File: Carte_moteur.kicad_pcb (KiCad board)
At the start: 2 copper layers, 94 parts, among them J101 Conn_01x02_Socket, J102 Conn_01x02, J103 Conn_01x02, J201 Conn_01x04_Pin, J301 Conn_01x04_Pin, J401 Conn_01x04_Pin, J601 Conn_01x06_Pin, J602 USB_B_Mini, Q601 MMBTA44, SW201 SW_DIP_x02, SW301 SW_DIP_x02, SW401 SW_DIP_x02, U101 LD1117S33TR_SOT223, U201 TMC2209, U301 TMC2209, U401 TMC2209, U501 STM32G474RETx, U601 ECMF02-2AMX6, U602 LD1117S33TR_SOT223, U603 STM32F103CBTx, Y601 Crystal_GND24

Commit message: Add net class
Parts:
- removed SW201, SW401: SW_DIP_x02, Button_Switch_THT:SW_DIP_SPSTx02_Slide_9.78x7.26mm_W7.62mm_P2.54mm
- added J104: Conn_01x07, Connector_Molex:Molex_KK-254_AE-6410-07A_1x07_P2.54mm_Vertical, F.Cu at (-344.4, -25.7)
- added J202: Conn_01x04_Pin, Connector_Molex:Molex_KK-254_AE-6410-04A_1x04_P2.54mm_Vertical, F.Cu at (-275.7, 52.7)
- added J302: Conn_01x04_Pin, Connector_Molex:Molex_KK-254_AE-6410-04A_1x04_P2.54mm_Vertical, F.Cu at (-299.4, 52.7)
- added J402: Conn_01x04_Pin, Connector_Molex:Molex_KK-254_AE-6410-04A_1x04_P2.54mm_Vertical, F.Cu at (-252.1, 52.7)
- added R101: R_US, Resistor_SMD:R_0603_1608Metric_Pad0.98x0.95mm_HandSolder, F.Cu at (-344.5, -20.5)
- added R102: R_US, Resistor_SMD:R_0603_1608Metric_Pad0.98x0.95mm_HandSolder, F.Cu at (-344.5, -18.0)
- added R103: R_US, Resistor_SMD:R_0603_1608Metric_Pad0.98x0.95mm_HandSolder, F.Cu at (-344.5, -15.5)
- added R104: R_US, Resistor_SMD:R_0603_1608Metric_Pad0.98x0.95mm_HandSolder, F.Cu at (-344.5, -13.0)
- added R105: R_US, Resistor_SMD:R_0603_1608Metric_Pad0.98x0.95mm_HandSolder, F.Cu at (-344.5, -10.5)
- added R206: R_US, Resistor_SMD:R_0805_2012Metric_Pad1.20x1.40mm_HandSolder, B.Cu at (-275.0, 19.4)
- added R207: R_US, Resistor_SMD:R_0603_1608Metric_Pad0.98x0.95mm_HandSolder, B.Cu at (-274.7, 33.9)
- added R306: R_US, Resistor_SMD:R_0805_2012Metric_Pad1.20x1.40mm_HandSolder, B.Cu at (-298.6, 19.4)
- added R307: R_US, Resistor_SMD:R_0603_1608Metric_Pad0.98x0.95mm_HandSolder, B.Cu at (-298.4, 33.9)
- added R406: R_US, Resistor_SMD:R_0805_2012Metric_Pad1.20x1.40mm_HandSolder, B.Cu at (-251.3, 19.4)
- added R407: R_US, Resistor_SMD:R_0603_1608Metric_Pad0.98x0.95mm_HandSolder, B.Cu at (-251.1, 33.9)
- added R512: R_US, Resistor_SMD:R_0603_1608Metric_Pad0.98x0.95mm_HandSolder, F.Cu at (-287.7, -15.3)
- added R513: R_US, Resistor_SMD:R_0603_1608Metric_Pad0.98x0.95mm_HandSolder, F.Cu at (-283.3, -25.4)
- added R514: R_US, Resistor_SMD:R_0603_1608Metric_Pad0.98x0.95mm_HandSolder, F.Cu at (-283.3, -22.9)
- added R515: R_US, Resistor_SMD:R_0603_1608Metric_Pad0.98x0.95mm_HandSolder, F.Cu at (-283.3, -20.4)
- added R516: R_US, Resistor_SMD:R_0603_1608Metric_Pad0.98x0.95mm_HandSolder, F.Cu at (-283.3, -17.8)
- added R517: R_US, Resistor_SMD:R_0603_1608Metric_Pad0.98x0.95mm_HandSolder, F.Cu at (-283.3, -15.3)
- added R518: R_US, Resistor_SMD:R_0805_2012Metric_Pad1.20x1.40mm_HandSolder, F.Cu at (-281.7, -12.6)
- added R519: R_US, Resistor_SMD:R_0805_2012Metric_Pad1.20x1.40mm_HandSolder, F.Cu at (-281.7, -9.66)
- added SW302: SW_DIP_x02, Button_Switch_THT:SW_DIP_SPSTx02_Slide_9.78x7.26mm_W7.62mm_P2.54mm, F.Cu at (-302.5, 19.6)
- added SW303: SW_DIP_x02, Button_Switch_THT:SW_DIP_SPSTx02_Slide_9.78x7.26mm_W7.62mm_P2.54mm, F.Cu at (-255.2, 19.6)
- C201, C202, C301, C302, C401, C402, R202, R205, R302, R305, R402, R405: moved to B.Cu
- C502: footprint Capacitor_SMD:C_0603_1608Metric_Pad1.08x0.95mm_HandSolder -> Capacitor_SMD:C_0805_2012Metric_Pad1.18x1.45mm_HandSolder
- C503: footprint Capacitor_SMD:C_0805_2012Metric_Pad1.18x1.45mm_HandSolder -> Capacitor_SMD:C_0603_1608Metric_Pad1.08x0.95mm_HandSolder
- J201, J301, J401: value Conn_01x04_Pin -> Conn_01x05_Pin; footprint Connector_Molex:Molex_KK-254_AE-6410-04A_1x04_P2.54mm_Vertical -> Connector_Molex:Molex_KK-254_AE-6410-05A_1x05_P2.54mm_Vertical
- R201, R204, R301, R304, R401, R404: footprint Resistor_SMD:R_0805_2012Metric_Pad1.20x1.40mm_HandSolder -> Resistor_SMD:R_0603_1608Metric_Pad0.98x0.95mm_HandSolder; moved to B.Cu
- R203, R303, R403: footprint Resistor_SMD:R_0603_1608Metric_Pad0.98x0.95mm_HandSolder -> Resistor_SMD:R_0805_2012Metric_Pad1.20x1.40mm_HandSolder; moved to B.Cu
- R509, R510, R511: footprint Resistor_SMD:R_0805_2012Metric_Pad1.20x1.40mm_HandSolder -> Resistor_SMD:R_0603_1608Metric_Pad0.98x0.95mm_HandSolder
- moved R511 221.2 mm to (-322.7, -23.3)
- moved R510 221.1 mm to (-322.7, -25.8)
- moved R509 221.0 mm to (-322.7, -28.3)
- moved C104 188.7 mm to (-301.8, -42.3)
- moved C506 183.5 mm to (-296.4, -15.3)
- moved C507 183.4 mm to (-292.0, -25.4)
- moved C505 183.4 mm to (-296.4, -17.8)
- moved C504 183.2 mm to (-296.4, -20.4)
- moved C503 183.1 mm to (-296.4, -22.9)
- moved R501 181.7 mm to (-292.0, -22.9)
- moved R504 181.7 mm to (-292.0, -15.3)
- moved R301 176.5 mm to (-303.9, 7.75), turned to 180 degrees
- moved C105 176.1 mm to (-286.5, -48.5)
- moved R302 171.5 mm to (-303.9, 11.3), turned to 180 degrees
- moved R304 168.8 mm to (-298.4, 31.4)
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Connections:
- net /micro/DIR1 renamed /micro/HRTIM_CHA2
- net /micro/DIR2 renamed /micro/HRTIM_CHB2
- net /micro/DIR3 renamed /micro/HRTIM_CHE2
- net /micro/SPI_MISO renamed /micro/SPI1_MISO
- net /micro/SPI_MOSI renamed /micro/SPI1_MOSI
- net /micro/SPI_SCK renamed /micro/SPI1_SCK
- net /micro/STEP1 renamed /micro/HRTIM_CHA1
- net /micro/STEP2 renamed /micro/HRTIM_CHB1
- net /micro/STEP3 renamed /micro/HRTIM_CHE1
- C502 pad 1: +3V3 -> Net-(U501-VREF+)
- C503 pad 1: Net-(U501-VREF+) -> +3V3
- J201 pad 1: /tmc_motor/A02 -> Net-(J201-Pin_1)
- J201 pad 2: /tmc_motor/A01 -> /micro/TIM1_CH1
- J201 pad 3: /tmc_motor/B01 -> /micro/TIM1_CH2
- J201 pad 4: /tmc_motor/B02 -> /micro/TIM1_ETR
- J301 pad 1: /tmc_motor1/A02 -> Net-(J301-Pin_1)
- J301 pad 2: /tmc_motor1/A01 -> /micro/TIM3_CH1
- J301 pad 3: /tmc_motor1/B01 -> /micro/TIM3_CH2
- J301 pad 4: /tmc_motor1/B02 -> /micro/TIM3_ETR
- J401 pad 1: /tmc_motor2/A02 -> Net-(J401-Pin_1)
- J401 pad 2: /tmc_motor2/A01 -> /micro/TIM5_CH1
- J401 pad 3: /tmc_motor2/B01 -> /micro/TIM5_CH2
- J401 pad 4: /tmc_motor2/B02 -> /micro/TIM5_ETR
- R201 pad 1: +3V3 -> Net-(J201-Pin_1)
- R201 pad 2: Net-(U201-MS1) -> +3V3
- R202 pad 1: Net-(U201-MS1) -> Net-(J201-Pin_1)
- R202 pad 2: GND -> +5V
- R203 pad 1: /micro/TMC1 -> +3V3
- R203 pad 2: Net-(R203-Pad2) -> Net-(U201-MS1)
- R204 pad 1: +3V3 -> Net-(U201-MS1)
- R204 pad 2: Net-(U201-MS2) -> GND
- R205 pad 1: Net-(U201-MS2) -> /micro/TMC1
- R205 pad 2: GND -> Net-(R205-Pad2)
- R301 pad 1: +3V3 -> Net-(J301-Pin_1)
- R301 pad 2: Net-(U301-MS1) -> +3V3
- R302 pad 1: Net-(U301-MS1) -> Net-(J301-Pin_1)
- R302 pad 2: GND -> +5V
- R303 pad 1: /micro/TMC2 -> +3V3
- R303 pad 2: Net-(R303-Pad2) -> Net-(U301-MS1)
- R304 pad 1: +3V3 -> Net-(U301-MS1)
- R304 pad 2: Net-(U301-MS2) -> GND
- R305 pad 1: Net-(U301-MS2) -> /micro/TMC2
- R305 pad 2: GND -> Net-(R305-Pad2)
- R401 pad 1: +3V3 -> Net-(J401-Pin_1)
- R401 pad 2: Net-(U401-MS1) -> +3V3
- R402 pad 1: Net-(U401-MS1) -> Net-(J401-Pin_1)
- R402 pad 2: GND -> +5V
- R403 pad 1: /micro/TMC3 -> +3V3
- R403 pad 2: Net-(R403-Pad2) -> Net-(U401-MS1)
- R404 pad 1: +3V3 -> Net-(U401-MS1)
- R404 pad 2: Net-(U401-MS2) -> GND
- R405 pad 1: Net-(U401-MS2) -> /micro/TMC3
- R405 pad 2: GND -> Net-(R405-Pad2)
- R501 pad 1: /stlink/T_NRST -> /micro/TIM1_CH1
- R502 pad 1: /micro/TMC3 -> /micro/TIM3_CH1
- R502 pad 2: /micro/UART1_TX -> +3V3
- R503 pad 1: /micro/TMC3 -> /micro/TIM5_CH1
- R503 pad 2: /micro/UART1_RX -> +3V3
- R504 pad 1: Net-(U501-VREF+) -> /micro/TIM1_CH2
- R505 pad 1: /micro/TMC1 -> /micro/TIM3_CH2
- R505 pad 2: /micro/UART2_TX -> +3V3
- R506 pad 1: /micro/TMC1 -> /micro/TIM5_CH2
- R506 pad 2: /micro/UART2_RX -> +3V3
- R507 pad 1: /micro/TMC2 -> /micro/TIM1_ETR
- R507 pad 2: /micro/UART3_TX -> +3V3
- R508 pad 1: /micro/TMC2 -> /micro/TIM3_ETR
- R508 pad 2: /micro/UART3_RX -> +3V3
- R509 pad 1: /micro/TMC1 -> /micro/TIM5_ETR
- R509 pad 2: Net-(R509-Pad2) -> +3V3
- R510 pad 1: /micro/TMC2 -> /micro/T_RST
- R510 pad 2: Net-(R509-Pad2) -> +3V3
- R511 pad 1: /micro/TMC3 -> Net-(U501-VREF+)
- R511 pad 2: Net-(R509-Pad2) -> +3V3
- SW301 pad 1: Net-(U301-MS1) -> Net-(U201-MS2)
- SW301 pad 2: Net-(U301-MS2) -> Net-(U201-MS1)
- U201 pad 4: Net-(R203-Pad2) -> Net-(R205-Pad2)
- U301 pad 4: Net-(R303-Pad2) -> Net-(R305-Pad2)
- U401 pad 4: Net-(R403-Pad2) -> Net-(R405-Pad2)
- U501 pad 12: unconnected-(U501-PA0-Pad12) -> /micro/TIM5_CH1
- U501 pad 13: unconnected-(U501-PA1-Pad13) -> /micro/TIM5_CH2
- U501 pad 17: /micro/UART2_RX -> /micro/LPUART1_RX
- U501 pad 18: unconnected-(U501-PA4-Pad18) -> /micro/TIM3_CH2
- U501 pad 33: /micro/UART3_RX -> /micro/LPUART1_TX
- U501 pad 34: unconnected-(U501-PB12-Pad34) -> /micro/TIM5_ETR
- U501 pad 38: unconnected-(U501-PC6-Pad38) -> /micro/TIM3_CH1
- U501 pad 46: unconnected-(U501-PA12-Pad46) -> /micro/TIM1_ETR
- U501 pad 49: /stlink/T_JTMS -> /micro/T_SWDIO
- U501 pad 50: /stlink/T_JTCK -> /micro/T_SWCLK
- U501 pad 51: /stlink/T_JTDI -> /micro/T_JDTI
- U501 pad 55: unconnected-(U501-PD2-Pad55) -> /micro/TIM3_ETR
- U501 pad 56: /stlink/T_SWO -> /micro/T_SWO
- U501 pad 57: unconnected-(U501-PB4-Pad57) -> /micro/UART2_RX
- U501 pad 61: unconnected-(U501-PB8-Pad61) -> /micro/UART3_RX
- U501 pad 7: /stlink/T_NRST -> /micro/T_RST
- U501 pad 8: /micro/LPUART1_RX -> /micro/TIM1_CH1
- U501 pad 9: /micro/LPUART1_TX -> /micro/TIM1_CH2
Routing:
- net GND: track 74.3 -> 148.1 mm
- net /tmc_motor2/A02: track 0.00 -> 52.3 mm
- net /tmc_motor2/A01: track 0.00 -> 43.3 mm
- net /tmc_motor2/B01: track 0.00 -> 35.7 mm
- net +3V3: track 0.00 -> 34.4 mm
- net Net-(U401-MS2): track 0.00 -> 30.7 mm
- net /tmc_motor2/B02: track 0.00 -> 26.4 mm
- net /tmc_motor1/A02: track 0.00 -> 26.2 mm
- net /tmc_motor/A02: track 0.00 -> 26.2 mm
- net Net-(U201-MS2): track 0.00 -> 25.3 mm
- net Net-(U301-MS2): track 0.00 -> 25.3 mm
- net Net-(U401-MS1): track 0.00 -> 23.8 mm
- net /tmc_motor1/A01: track 0.00 -> 21.7 mm
- net /tmc_motor/A01: track 0.00 -> 21.7 mm
- net Net-(U301-MS1): track 0.00 -> 18.2 mm
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
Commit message: move encoder pull up resistor to tmc sheet
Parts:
- removed R501, R502, R503, R504, R505, R506, R507, R508, R509: R_US, Resistor_SMD:R_0603_1608Metric_Pad0.98x0.95mm_HandSolder
- added R210: R_US, Resistor_SMD:R_0603_1608Metric_Pad0.98x0.95mm_HandSolder, B.Cu at (93.0, 135.1)
- added R211: R_US, Resistor_SMD:R_0603_1608Metric_Pad0.98x0.95mm_HandSolder, B.Cu at (95.5, 135.1)
- added R212: R_US, Resistor_SMD:R_0603_1608Metric_Pad0.98x0.95mm_HandSolder, B.Cu at (98.1, 135.1)
- added R523: R_US, Resistor_SMD:R_0603_1608Metric_Pad0.98x0.95mm_HandSolder, B.Cu at (120.5, 134.9)
- added R524: R_US, Resistor_SMD:R_0603_1608Metric_Pad0.98x0.95mm_HandSolder, B.Cu at (123.1, 134.9)
- added R525: R_US, Resistor_SMD:R_0603_1608Metric_Pad0.98x0.95mm_HandSolder, B.Cu at (125.6, 134.9)
- added R526: R_US, Resistor_SMD:R_0603_1608Metric_Pad0.98x0.95mm_HandSolder, B.Cu at (146.8, 134.8)
- added R527: R_US, Resistor_SMD:R_0603_1608Metric_Pad0.98x0.95mm_HandSolder, B.Cu at (149.4, 134.8)
- added R528: R_US, Resistor_SMD:R_0603_1608Metric_Pad0.98x0.95mm_HandSolder, B.Cu at (151.9, 134.8)
- R101, R102, R103, R104, R105: moved to B.Cu
- moved R608 511.0 mm to (115.5, 97.8), turned to 0 degrees
- moved C608 510.1 mm to (118.2, 104.1), turned to 180 degrees
- moved R607 509.9 mm to (115.5, 99.3), turned to 180 degrees
- moved R609 508.9 mm to (115.5, 100.8), turned to 0 degrees
- moved C605 507.8 mm to (115.5, 102.3), turned to 180 degrees
- moved Y601 507.7 mm to (117.8, 106.8), turned to -90 degrees
- moved C609 505.5 mm to (117.5, 109.4), turned to 0 degrees
- moved R613 500.8 mm to (113.2, 108.4), turned to 180 degrees
- moved R610 500.2 mm to (106.1, 96.7), turned to 180 degrees
- moved C607 499.8 mm to (109.4, 103.1), turned to 180 degrees
- moved R614 499.6 mm to (113.2, 110.2), turned to 180 degrees
- moved C603 498.7 mm to (109.4, 104.6), turned to 180 degrees
- moved U603 497.7 mm to (107.8, 103.4), turned to 180 degrees
- moved C606 496.4 mm to (106.1, 102.1), turned to 0 degrees
- moved D601 495.6 mm to (101.2, 95.0), turned to 90 degrees
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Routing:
- net +3V3: track 34.4 -> 156.9 mm
- net +BATT: track 15.7 -> 63.2 mm
- net /micro/T_JDTI: track 0.00 -> 40.5 mm, vias 0 -> 1
- net /micro/T_SWDIO: track 0.00 -> 38.1 mm, vias 0 -> 2
- net /micro/T_SWO: track 0.00 -> 34.8 mm, vias 0 -> 2
- net /micro/T_SWCLK: track 0.00 -> 33.6 mm, vias 0 -> 2
- net GND: track 148.1 -> 120.7 mm
- net /tmc_motor2/A02: track 52.3 -> 25.1 mm
- net /tmc_motor2/A01: track 43.3 -> 21.0 mm
- net /stlink/T_SWO: track 0.00 -> 19.9 mm, vias 0 -> 1
- net /tmc_motor2/B01: track 35.7 -> 16.9 mm
- net /stlink/T_JTMS: track 3.19 -> 21.5 mm, vias 0 -> 1
- net Net-(U401-MS2): track 30.7 -> 15.5 mm
- net /stlink/T_NRST: track 3.21 -> 17.9 mm, vias 0 -> 1
- net /tmc_motor2/B02: track 26.4 -> 12.8 mm
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
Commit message: hrtim
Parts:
- removed R205, R305, R405: R_US, Resistor_SMD:R_0603_1608Metric_Pad0.98x0.95mm_HandSolder
- moved R517 46.8 mm to (186.9, 117.1)
- moved R516 44.6 mm to (180.6, 114.6)
- moved R518 36.1 mm to (154.2, 110.0)
- moved C502 36.1 mm to (159.5, 117.9)
- moved R519 36.1 mm to (159.5, 114.9)
- moved R513 30.8 mm to (145.4, 85.6)
- moved R512 23.7 mm to (144.8, 89.2)
- moved R406 10.6 mm to (147.2, 136.8), turned to 180 degrees
- moved R306 8.55 mm to (118.9, 136.8), turned to 180 degrees
- moved R206 8.41 mm to (91.2, 136.8), turned to 180 degrees
- moved R403 8.34 mm to (147.2, 139.3), turned to 180 degrees
- moved R514 8.07 mm to (175.8, 67.3)
- moved R515 8.07 mm to (175.8, 69.8)
- moved SW303 7.97 mm to (143.7, 136.8), turned to 0 degrees
- moved U501 6.62 mm to (129.5, 105.2), turned to 45 degrees
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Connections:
- U201 pad 4: Net-(R205-Pad2) -> /micro/TMC1
- U301 pad 4: Net-(R305-Pad2) -> /micro/TMC2
- U401 pad 4: Net-(R405-Pad2) -> /micro/TMC3
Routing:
- net GND: track 120.7 -> 260.7 mm
- net /micro/HRTIM_CHA2: track 0.00 -> 126.3 mm, vias 0 -> 3
- net /micro/HRTIM_CHA1: track 0.00 -> 123.8 mm, vias 0 -> 3
- net +BATT: track 63.2 -> 164.4 mm
- net /micro/HRTIM_CHB2: track 0.00 -> 100.1 mm, vias 0 -> 3
- net /micro/HRTIM_CHB1: track 0.00 -> 93.7 mm, vias 0 -> 3
- net /micro/HRTIM_CHE2: track 0.00 -> 71.3 mm, vias 0 -> 1
- net /micro/HRTIM_CHE1: track 0.00 -> 68.2 mm, vias 0 -> 1
- net /micro/TIM1_CH1: track 3.16 -> 36.9 mm, vias 0 -> 2
- net /micro/TIM1_CH2: track 3.16 -> 35.2 mm, vias 0 -> 2
- net /micro/TMC3: track 0.00 -> 30.6 mm, vias 0 -> 1
- net /micro/TMC2: track 0.00 -> 30.4 mm, vias 0 -> 1
- net /micro/TMC1: track 0.00 -> 30.3 mm, vias 0 -> 1
- net +3V3: track 156.9 -> 139.0 mm, vias 0 -> 1
- net /micro/TIM5_CH1: track 3.16 -> 15.6 mm, vias 0 -> 2
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
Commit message: AHHHAHAHAHHAH
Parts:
- added J105: Conn_01x02_Socket, Connector_Molex:Molex_KK-396_A-41791-0002_1x02_P3.96mm_Vertical, F.Cu at (166.6, 119.9)
- moved R514 70.7 mm to (122.2, 113.4), turned to 90 degrees
- moved R515 67.9 mm to (123.7, 113.4), turned to 90 degrees
- moved R517 54.3 mm to (136.4, 97.3), turned to 180 degrees
- moved R511 48.4 mm to (126.7, 114.8), turned to 90 degrees
- moved R516 48.2 mm to (136.4, 95.2), turned to 180 degrees
- moved C504 26.0 mm to (138.9, 107.0), turned to 90 degrees
- moved R513 24.1 mm to (123.7, 96.0), turned to -90 degrees
- moved R512 23.9 mm to (121.9, 96.0), turned to -90 degrees
- moved C503 16.8 mm to (122.8, 89.7), turned to 180 degrees
- moved R519 12.7 mm to (146.8, 115.6)
- moved C506 12.3 mm to (127.0, 95.0), turned to 90 degrees
- moved C505 11.9 mm to (131.8, 95.0), turned to 90 degrees
- moved C502 9.99 mm to (149.6, 119.1)
- moved J101 9.68 mm to (166.7, 108.9)
- moved C602 7.80 mm to (84.3, 103.3)
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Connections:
- J301 pad 2: /micro/TIM3_CH1 -> /micro/TIM5_CH1
- J301 pad 3: /micro/TIM3_CH2 -> /micro/TIM5_CH2
- J301 pad 4: /micro/TIM3_ETR -> /micro/TIM5_ETR
- J401 pad 2: /micro/TIM5_CH1 -> /micro/TIM3_CH1
- J401 pad 3: /micro/TIM5_CH2 -> /micro/TIM3_CH2
- J401 pad 4: /micro/TIM5_ETR -> /micro/TIM3_ETR
- R514 pad 1: /micro/TMC3 -> /micro/TMC2
- R515 pad 1: /micro/TMC3 -> /micro/TMC2
- R516 pad 1: /micro/TMC2 -> /micro/TMC3
- R517 pad 1: /micro/TMC2 -> /micro/TMC3
- R523 pad 1: /micro/TIM3_CH1 -> /micro/TIM5_CH1
- R524 pad 1: /micro/TIM3_CH2 -> /micro/TIM5_CH2
- R525 pad 1: /micro/TIM3_ETR -> /micro/TIM5_ETR
- R526 pad 1: /micro/TIM5_CH1 -> /micro/TIM3_CH1
- R527 pad 1: /micro/TIM5_CH2 -> /micro/TIM3_CH2
- R528 pad 1: /micro/TIM5_ETR -> /micro/TIM3_ETR
- U301 pad 7: /micro/HRTIM_CHB1 -> /micro/HRTIM_CHE1
- U301 pad 8: /micro/HRTIM_CHB2 -> /micro/HRTIM_CHE2
- U401 pad 7: /micro/HRTIM_CHE1 -> /micro/HRTIM_CHB1
- U401 pad 8: /micro/HRTIM_CHE2 -> /micro/HRTIM_CHB2
- U501 pad 30: /micro/UART3_TX -> unconnected-(U501-PB10-Pad30)
- U501 pad 62: unconnected-(U501-PB9-Pad62) -> /micro/UART3_TX
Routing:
- net +3V3: track 139.0 -> 61.1 mm, vias 1 -> 0
- net /micro/TIM1_ETR: track 3.16 -> 60.9 mm
- net +BATT: track 164.4 -> 110.8 mm
- net GND: track 260.7 -> 208.0 mm
- net /micro/HRTIM_CHB2: track 100.1 -> 58.2 mm, vias 3 -> 1
- net /micro/TIM3_ETR: track 3.27 -> 43.3 mm
- net /micro/HRTIM_CHB1: track 93.7 -> 56.5 mm, vias 3 -> 1
- net /micro/TMC3: track 30.6 -> 63.3 mm
- net /micro/T_JDTI: track 33.7 -> 2.64 mm
- net /micro/TMC2: track 30.4 -> 0.00 mm, vias 1 -> 0
- net /micro/TMC1: track 30.3 -> 0.00 mm, vias 1 -> 0
- net /micro/T_SWO: track 31.0 -> 2.54 mm, vias 2 -> 0
- net /micro/T_SWDIO: track 30.5 -> 2.64 mm, vias 2 -> 0
- net /micro/TIM1_CH1: track 36.9 -> 63.1 mm, vias 2 -> 1
- net /micro/TIM3_CH1: track 3.16 -> 27.8 mm, vias 1 -> 0
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
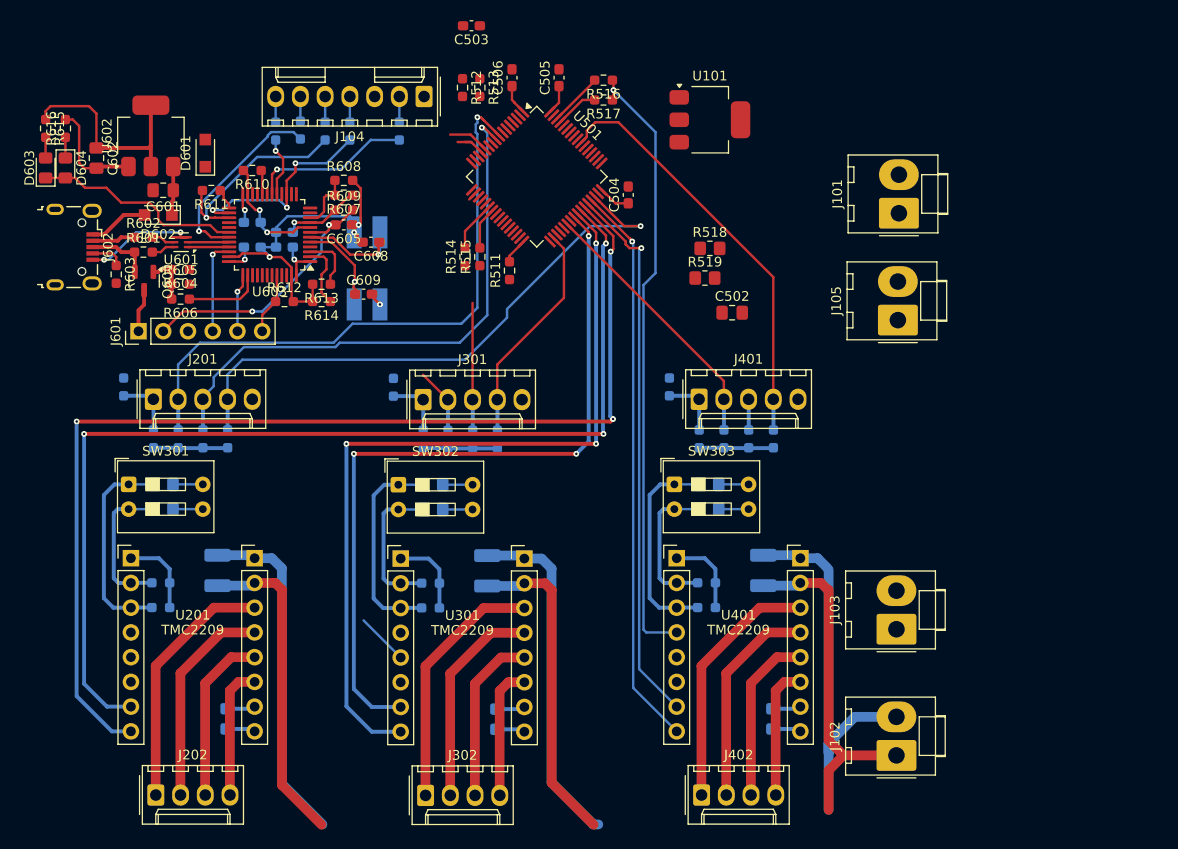
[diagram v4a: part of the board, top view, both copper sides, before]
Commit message: reduced stlink size
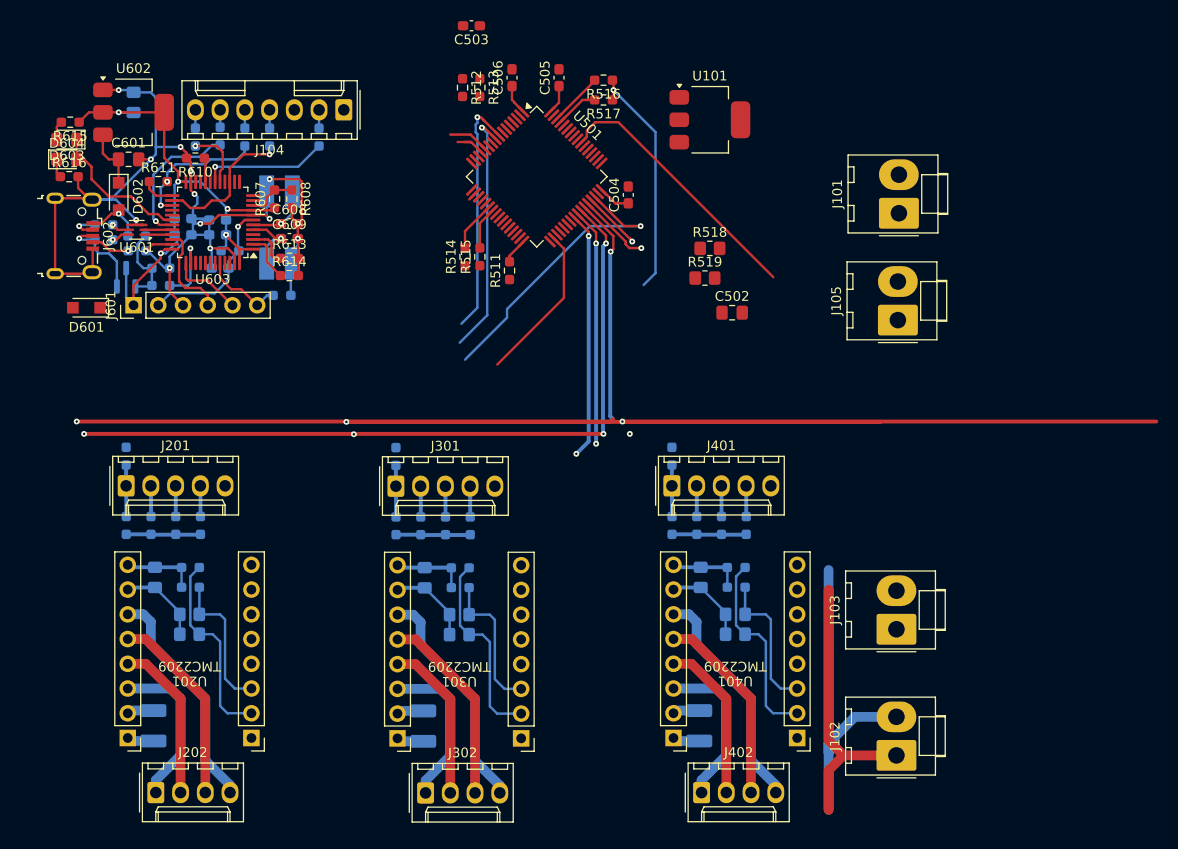
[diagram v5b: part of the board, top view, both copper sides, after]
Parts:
- removed SW301, SW302, SW303: SW_DIP_x02, Button_Switch_THT:SW_DIP_SPSTx02_Slide_9.78x7.26mm_W7.62mm_P2.54mm
- C602, C605, Q601, R601, R602, R603, R604, R605, R606, R609, R612: moved to B.Cu
- moved D601 20.0 mm to (83.3, 118.6), turned to 180 degrees
- moved C201 17.3 mm to (90.2, 161.5), turned to 90 degrees
- moved C301 17.3 mm to (117.9, 161.6), turned to 90 degrees
- moved C401 17.3 mm to (146.2, 161.5), turned to 90 degrees
- moved C402 16.3 mm to (146.4, 146.3), turned to 90 degrees
- moved C202 16.3 mm to (90.3, 146.3), turned to 90 degrees
- moved C302 16.3 mm to (118.0, 146.3), turned to 90 degrees
- moved R406 13.6 mm to (149.9, 150.1), turned to 0 degrees
- moved R206 13.6 mm to (93.9, 150.1), turned to 0 degrees
- moved R306 13.6 mm to (121.6, 150.1), turned to 0 degrees
- moved C605 13.5 mm to (97.0, 114.6), turned to 0 degrees
- moved R403 13.1 mm to (149.9, 152.1), turned to 0 degrees
- moved R203 13.1 mm to (93.9, 152.1), turned to 0 degrees
- moved R303 13.1 mm to (121.6, 152.2), turned to 0 degrees
- moved R609 12.4 mm to (98.0, 112.8)
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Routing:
- net /micro/HRTIM_CHA2: track 113.7 -> 188.1 mm, vias 3 -> 4
- net +BATT: track 110.8 -> 41.0 mm
- net /micro/HRTIM_CHE2: track 83.6 -> 24.4 mm, vias 3 -> 2
- net /micro/HRTIM_CHE1: track 78.0 -> 25.4 mm, vias 3 -> 2
- net /micro/HRTIM_CHB2: track 58.2 -> 6.15 mm
- net /micro/HRTIM_CHB1: track 56.5 -> 7.78 mm
- net /micro/TMC3: track 63.3 -> 24.4 mm
- net /micro/TIM1_CH1: track 63.1 -> 28.7 mm
- net /micro/HRTIM_CHA1: track 108.9 -> 77.5 mm, vias 3 -> 5
- net /micro/TIM1_CH2: track 58.2 -> 29.0 mm
- net /micro/TIM1_ETR: track 60.9 -> 33.3 mm
- net /micro/TIM3_CH1: track 27.8 -> 3.14 mm
- net GND: track 208.0 -> 184.6 mm, vias 8 -> 14
- net +3.3VA: track 44.5 -> 60.3 mm, vias 4 -> 5
- net /micro/TIM3_ETR: track 43.3 -> 30.7 mm
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
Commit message: before trying new µC orientation
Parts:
- removed C502: C, Capacitor_SMD:C_0805_2012Metric_Pad1.18x1.45mm_HandSolder
- added C508: C, Capacitor_SMD:C_0603_1608Metric_Pad1.08x0.95mm_HandSolder, F.Cu at (102.1, 82.0)
- added J106: Conn_01x07, Connector_Molex:Molex_KK-254_AE-6410-07A_1x07_P2.54mm_Vertical, F.Cu at (88.4, 103.4)
- C101, C102, C104: moved to B.Cu
- moved C101 127.7 mm to (89.2, 151.6), turned to 90 degrees
- moved C102 116.0 mm to (108.2, 151.6), turned to 90 degrees
- moved C103 110.0 mm to (70.1, 94.7), turned to 90 degrees
- moved C104 106.5 mm to (127.5, 151.6), turned to 90 degrees
- moved C105 105.8 mm to (73.2, 94.7), turned to 90 degrees
- moved J101 86.8 mm to (83.3, 132.9), turned to -90 degrees
- moved J102 83.9 mm to (83.1, 155.2), turned to -90 degrees
- moved J103 83.5 mm to (83.2, 146.1), turned to -90 degrees
- moved J105 83.4 mm to (83.3, 123.7), turned to -90 degrees
- moved U101 75.0 mm to (72.4, 102.4), turned to -90 degrees
- moved R615 64.7 mm to (144.2, 115.8), turned to 0 degrees
- moved D603 64.6 mm to (144.6, 114.0), turned to 0 degrees
- moved D604 63.9 mm to (144.6, 111.9), turned to 180 degrees
- moved D601 63.2 mm to (142.6, 96.7), turned to 0 degrees
- moved R616 63.0 mm to (144.3, 110.2), turned to 180 degrees
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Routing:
- net /micro/HRTIM_CHA2: track 188.1 -> 16.1 mm, vias 4 -> 1
- net /micro/TMC1: track 0.00 -> 69.4 mm, vias 0 -> 1
- net /micro/TIM3_CH2: track 4.25 -> 64.9 mm, vias 0 -> 2
- net /micro/HRTIM_CHA1: track 77.5 -> 17.1 mm, vias 5 -> 1
- net /micro/TMC2: track 0.00 -> 56.8 mm, vias 0 -> 2
- net /micro/TIM5_CH2: track 6.98 -> 58.6 mm, vias 0 -> 4
- net /micro/TIM5_CH1: track 7.42 -> 57.4 mm, vias 0 -> 4
- net /micro/TMC3: track 24.4 -> 73.1 mm, vias 1 -> 2
- net /micro/HRTIM_CHB2: track 6.15 -> 51.1 mm, vias 1 -> 2
- net /micro/HRTIM_CHB1: track 7.78 -> 52.2 mm, vias 1 -> 2
- net /tmc_motor2/B02: track 23.6 -> 68.0 mm
- net /micro/TIM3_CH1: track 3.14 -> 45.4 mm, vias 0 -> 2
- net /tmc_motor2/B01: track 20.1 -> 60.4 mm
- net /tmc_motor2/A01: track 16.6 -> 49.7 mm
- net /tmc_motor2/A02: track 16.6 -> 49.7 mm
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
